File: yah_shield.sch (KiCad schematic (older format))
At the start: 1 part

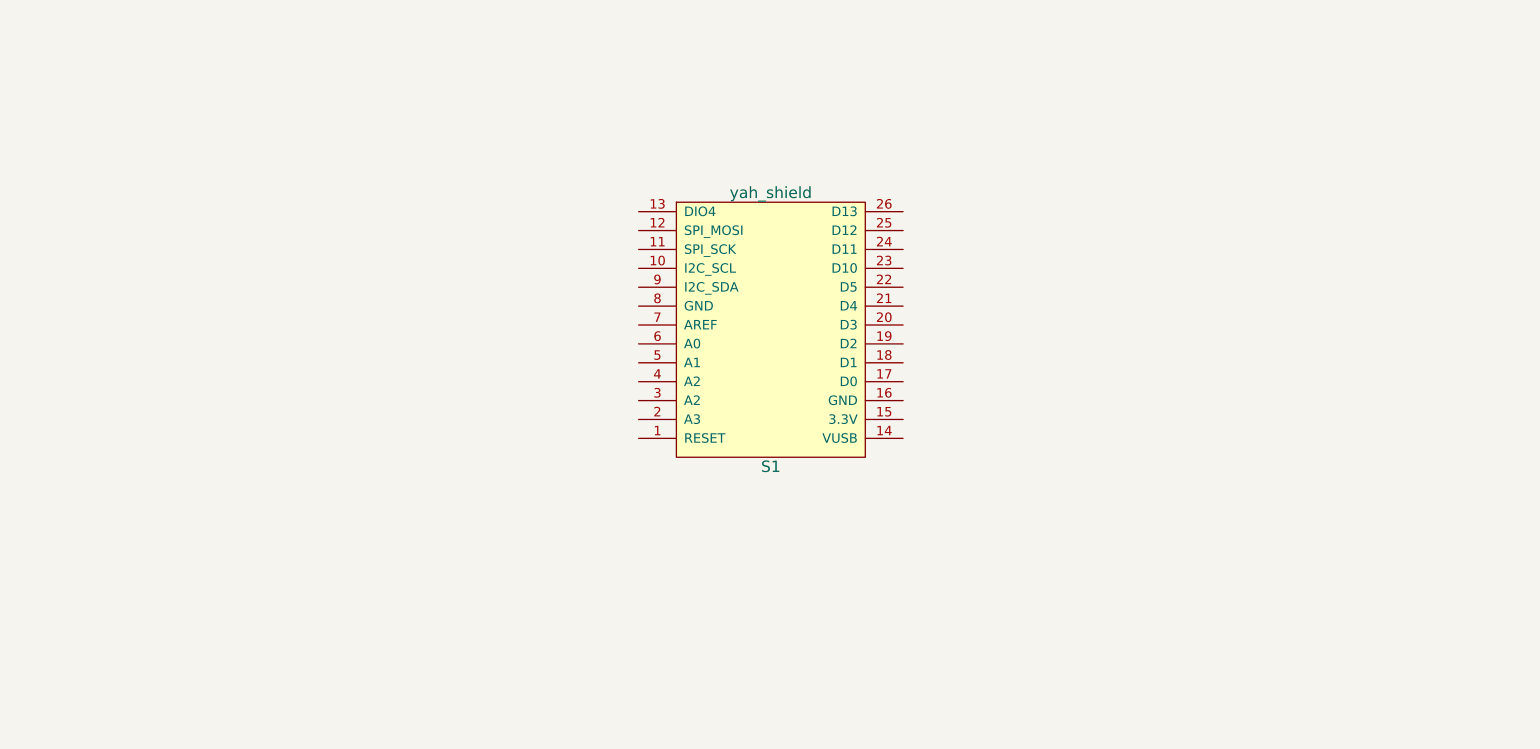
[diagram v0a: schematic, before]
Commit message: Add tps61096a and ina226
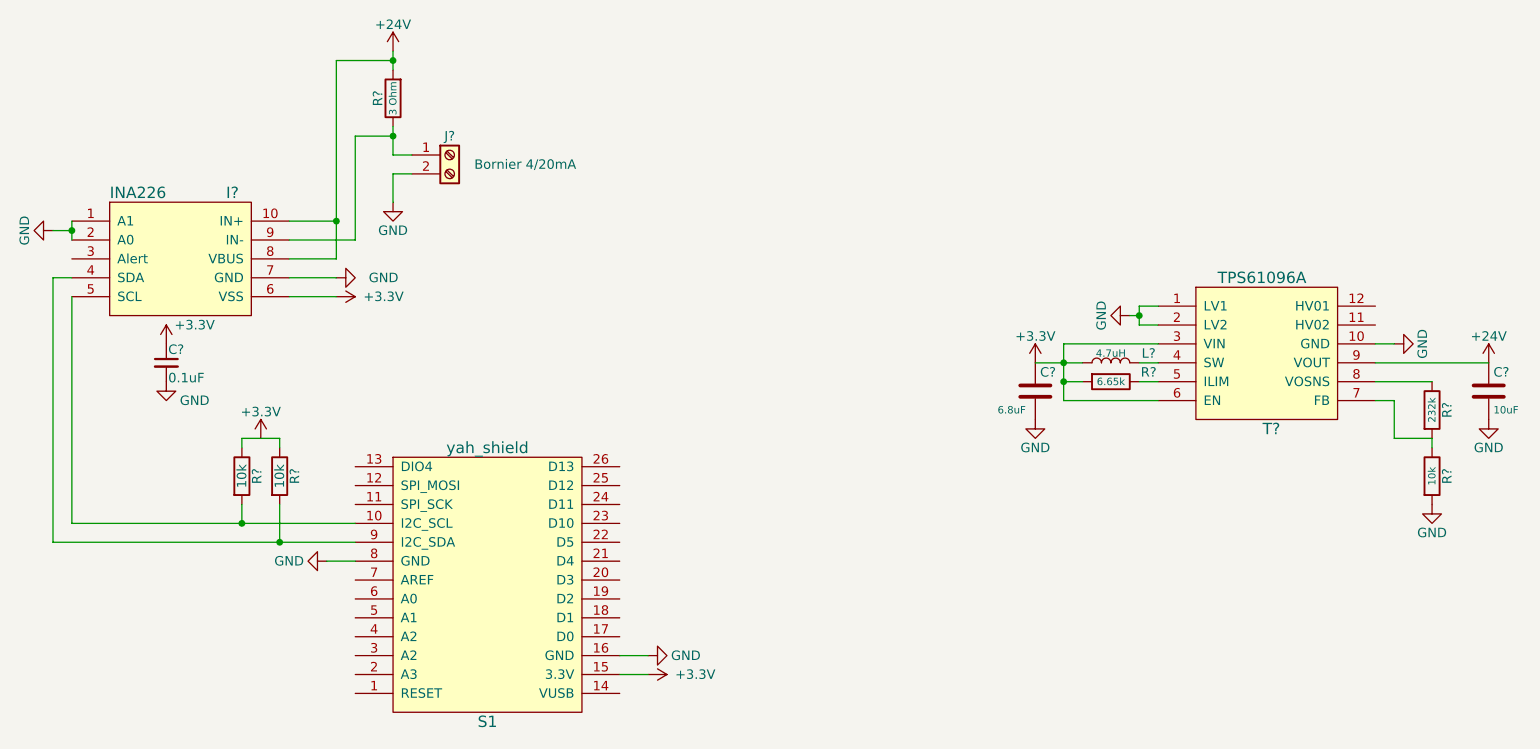
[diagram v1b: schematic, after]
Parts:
- added C?: 0.1uF, symbol C_Small
- added C?: 10uF, symbol C
- added C?: 6.8uF, symbol C
- added I?: INA226, symbol INA226
- added J?: Bornier 4/20mA, symbol Screw_Terminal_01x02
- added L?: 4.7uH, symbol L
- added R? (x3): 10k, symbol R
- added R?: 3 Ohm, symbol R
- added R?: 232k, symbol R
- added R?: 6.65k, symbol R
- added T?: TPS61096A, symbol TPS61096A
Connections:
- net at S1.10 (I2C_SCL): now also I?.5 (SCL), R?.2
- net +3V3: now reaches S1.15 (3.3V)
- net +3V3: now also C?.1, C?.1, I?.6 (VSS), L?.1, R?.2, T?.3 (VIN), T?.6 (EN)
- net GND: now reaches S1.16 (GND)
- net GND: now also S1.8 (GND), C?.2, C?.2, C?.2, I?.1 (A1), I?.2 (A0), I?.7 (GND), J?.2 (Pin_2), R?.2, T?.1 (LV1), T?.10 (GND), T?.2 (LV2)
- net at S1.9 (I2C_SDA): now also I?.4 (SDA), R?.2
- new net: I?.9 (IN-), J?.1 (Pin_1), R?.1
- new net: R?.1, R?.1
- new net: L?.2, T?.4 (SW)
- new net: R?.1, T?.5 (ILIM)
- new net: R?.1, R?.2, T?.7 (FB)
- new net: R?.1, T?.8 (VOSNS)
- new net +24V: C?.1, I?.10 (IN+), I?.8 (VBUS), R?.2, T?.9 (VOUT)
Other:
- moved on the sheet: S1
